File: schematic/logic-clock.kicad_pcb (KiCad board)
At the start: 2 copper layers, 65 parts, among them P11 3-PIN_HEADER, P12 2-PIN_HEADER, P13 3-PIN_HEADER, P14 1-PIN_HEADER, P15 4-PIN_HEADER, P16 4-PIN_HEADER, P17 4-PIN_HEADER, P18 4-PIN_HEADER, P19 4-PIN_HEADER, P20 3-PIN_HEADER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

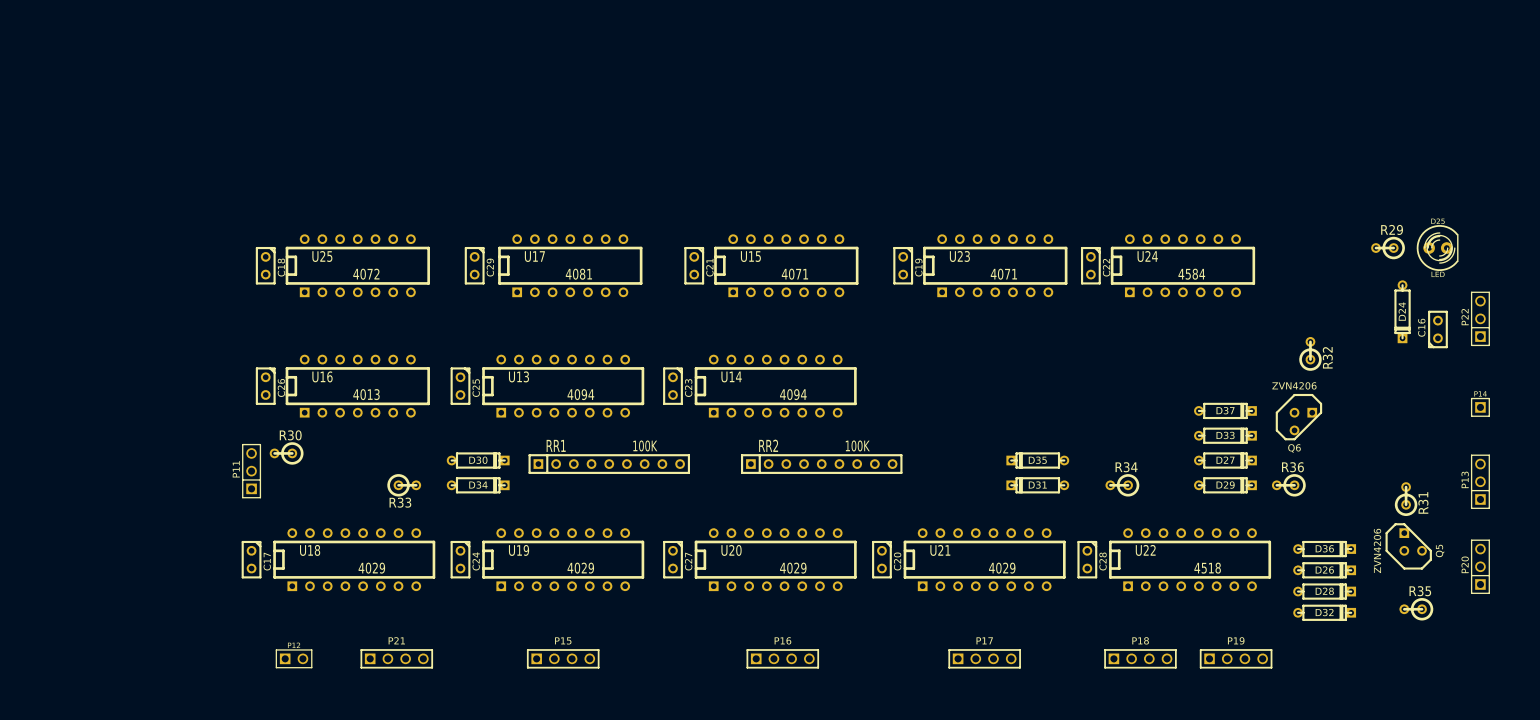
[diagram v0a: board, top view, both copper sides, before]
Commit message: half laid out, fixed netlist again
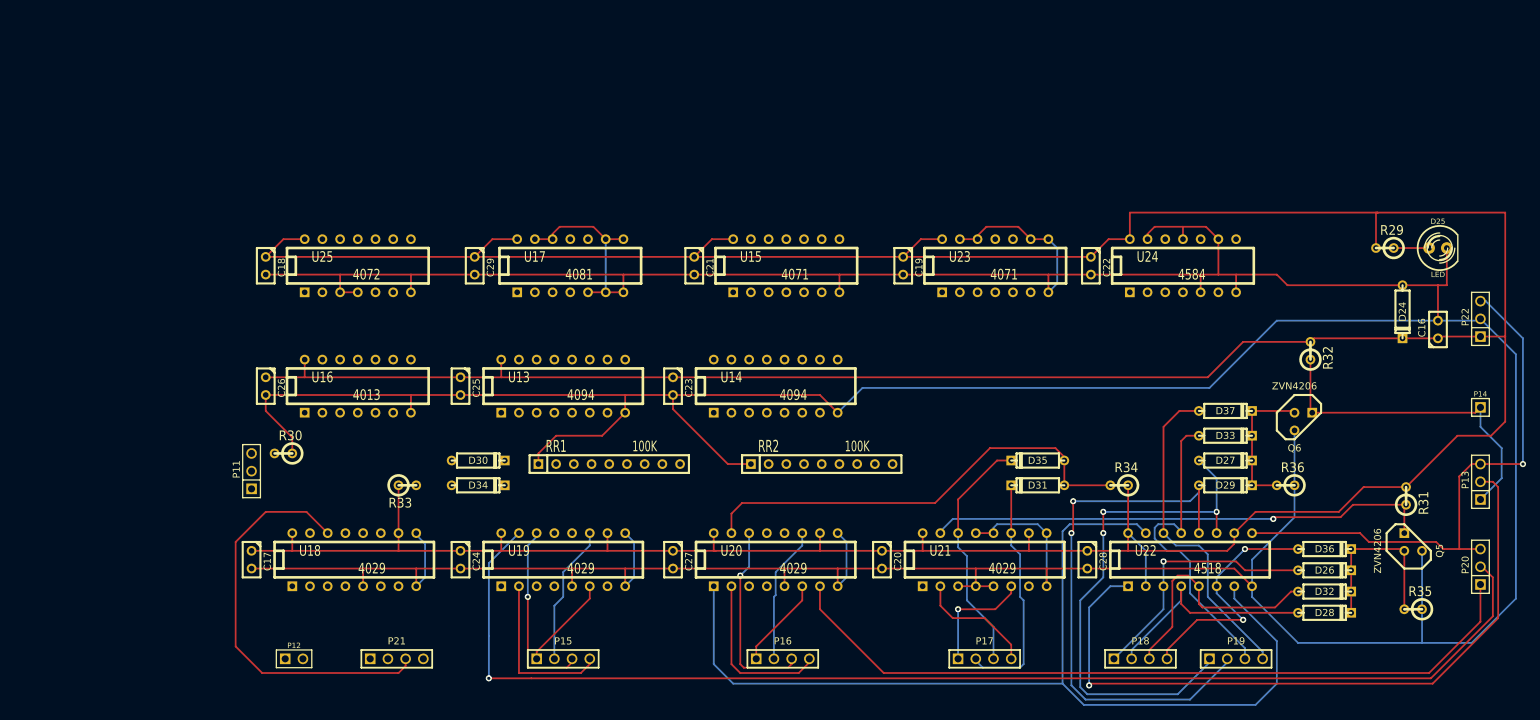
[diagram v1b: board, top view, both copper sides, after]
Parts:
- moved D28 3.05 mm to (231.6, 154.9)
- moved D32 3.05 mm to (231.6, 151.9)
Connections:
- U16 pad 10: N-00000259 -> N-00000188
- U16 pad 11: GND -> N-00000221
- U16 pad 12: (no net) -> N-00000208
- U16 pad 13: N-00000264 -> /comparator-board/AM
- U16 pad 8: N-00000261 -> N-00000189
- U16 pad 9: GND -> N-00000208
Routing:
- net GND: track 0.00 -> 839.3 mm
- net +5V: track 0.00 -> 664.2 mm
- net /logic-board/TEN-MIN_CLOCK: track 0.00 -> 178.3 mm, vias 0 -> 1
- net SET: track 0.00 -> 146.9 mm
- net /logic-board/MIN-CARRY: track 0.00 -> 110.2 mm
- net /logic-board/SEC_CLOCK: track 0.00 -> 102.4 mm, vias 0 -> 1
- net /logic-board/10Hz: track 0.00 -> 80.3 mm, vias 0 -> 1
- net /display-board/0B: track 0.00 -> 78.9 mm, vias 0 -> 2
- net /display-board/0A: track 0.00 -> 75.6 mm, vias 0 -> 3
- net N-00000233: track 0.00 -> 72.8 mm, vias 0 -> 1
- net N-00000227: track 0.00 -> 65.6 mm
- net /comparator-board/5C: track 0.00 -> 58.6 mm
- net 1Hz: track 0.00 -> 47.9 mm
- net /display-board/0D: track 0.00 -> 47.1 mm
- net /display-board/0C: track 0.00 -> 46.0 mm
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
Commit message: about to try some sort of autorouter
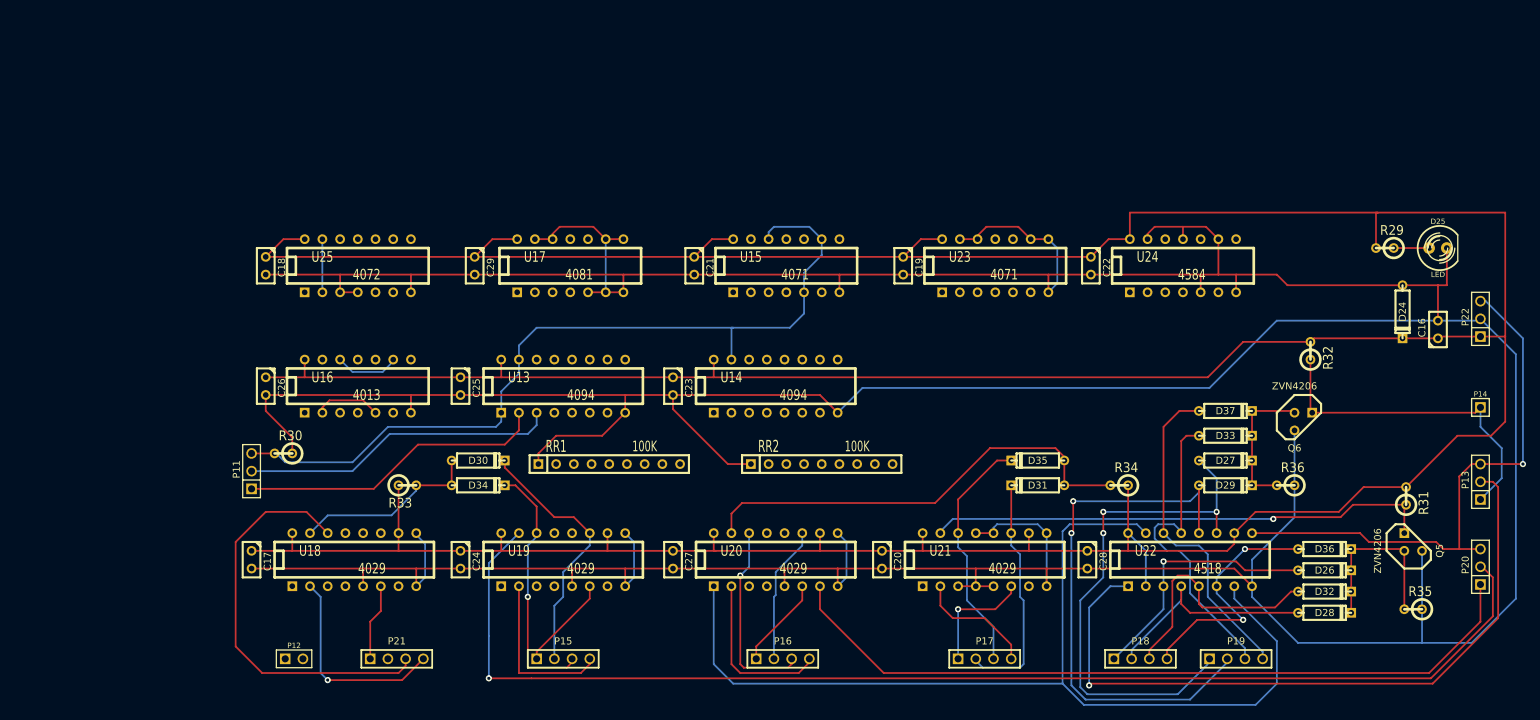
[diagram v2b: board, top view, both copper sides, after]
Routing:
- net SET: track 146.9 -> 266.6 mm
- net /logic-board/CLOCK: track 0.00 -> 45.4 mm
- net /logic-board/DATA: track 0.00 -> 44.4 mm
- net /comparator-board/5D: track 0.00 -> 29.5 mm, vias 0 -> 1
- net TEN-MIN_CARRY: track 0.00 -> 27.2 mm
- net /comparator-board/4B: track 20.1 -> 37.2 mm
- net /comparator-board/5A: track 0.00 -> 11.0 mm
- net /comparator-board/4C: track 27.0 -> 36.6 mm
- net N-00000210: track 0.00 -> 9.54 mm
- net N-00000208: track 0.00 -> 9.24 mm
- net N-00000205: track 0.00 -> 7.62 mm
- net +5V: track 664.2 -> 666.8 mm

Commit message: ready for autorouter
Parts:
- moved P16 37.8 mm to (125.5, 136.7)
- moved P17 37.8 mm to (154.4, 136.7)
- moved P18 37.8 mm to (176.8, 136.7)
- moved P19 37.8 mm to (190.5, 136.7)
- moved P21 37.8 mm to (70.1, 136.7)
- moved C19 37.8 mm to (142.7, 80.3)
- moved C22 37.8 mm to (169.7, 80.3)
- moved D24 37.8 mm to (214.4, 86.9)
- moved D27 37.8 mm to (189.0, 108.2)
- moved D30 37.8 mm to (81.8, 108.2)
- moved D35 37.8 mm to (162.1, 108.2)
- moved P12 37.8 mm to (55.4, 136.7)
- moved P13 37.8 mm to (225.6, 111.3)
- moved P15 37.8 mm to (94.0, 136.7)
- moved P20 37.8 mm to (225.6, 123.4)
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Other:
- board outline added: 191 x 77.2 mm
